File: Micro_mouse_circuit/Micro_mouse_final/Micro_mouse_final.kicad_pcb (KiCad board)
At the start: 2 copper layers, 77.3 x 75 mm, 51 parts, among them J1 Conn_01x02, J2 USB_C_Receptacle_PowerOnly_6P, J3 Conn_02x16_Odd_Even, U1 INA219AxDCN, U10 SN74LVC1G3157DCKR, U11 TPS22917DBVR, U13 TPS22917DBVR, U2 AMS1117-3.3, U3 HUSB237-AA001-DN06R, U4 MT3608, U5 LM2596SX-5_0/NOPB, U6 SK22D15L5, U7 L298N_C19922, U8 L298N_C19922, U9 TP4056_C382139

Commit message: common share
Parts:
- added R9: 0, xxcustom_footprint:C1206, F.Cu at (161.0, 103.5)
- L1: value 10uH -> 10u
- R10: value 0805W8F4702T5E -> 47k
- R12: footprint xxcustom_footprint:C1206 -> xxcustom_footprint:R1206
- R14, R16: footprint xxcustom_footprint:R0402 -> xxcustom_footprint:R1206
- R15: value 6k -> 5.6k
- R3: value 0603WAF7502T5E -> 75k
- R4: value 0805W8F2702T5E -> 27k
- moved C3 28.2 mm to (188.0, 101.0)
- moved REF1 0.50 mm to (150.0, 76.5)
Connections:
- D2 pad 1: Net-(D2-K) -> /SwitchCommon
- L2 pad 1: Net-(D2-K) -> /SwitchCommon
- U5 pad 2: Net-(D2-K) -> /SwitchCommon
- U9 pad 4: Net-(U9-VCC) -> /5V
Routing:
- net GND: track 80.0 -> 0.00 mm
- net /9V: track 46.1 -> 0.00 mm
- net /5V: track 39.8 -> 0.00 mm
- net Net-(D2-K): track 31.5 -> 0.00 mm
- net /BatteryPos: track 26.2 -> 0.00 mm
- net /SwitchOn: track 18.2 -> 0.00 mm
- net Net-(J1-Pin_1): track 14.2 -> 0.00 mm
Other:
- outline, holes or cut-outs redrawn

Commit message: push  - kt
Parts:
- removed REF1: high_frequency_680uF35V, xxcustom_footprint:CAP-TH_BD10.0-P5.00-D1.0-FD
- added C2: 680u, xxcustom_footprint:CAP-TH_BD8.0-P3.50-D0.6-FD, F.Cu at (150.0, 77.0)
- added R11: 1, xxcustom_footprint:R1206, F.Cu at (170.8, 137.6)
- added R13: 1, xxcustom_footprint:R1206, F.Cu at (170.8, 141.0)
- added R9: 1, xxcustom_footprint:R1206, F.Cu at (170.8, 134.3)
- added TP6: TestPoint, TestPoint:TestPoint_Pad_2.5x2.5mm, F.Cu at (163.0, 87.0)
- added TP7: TestPoint, TestPoint:TestPoint_Pad_2.5x2.5mm, F.Cu at (163.0, 91.5)
- added TP8: TestPoint, TestPoint:TestPoint_Pad_2.5x2.5mm, F.Cu at (176.0, 134.9)
- added TP9: TestPoint, TestPoint:TestPoint_Pad_2.5x2.5mm, F.Cu at (176.0, 139.5)
- C1: value CL31B105KBHNNNE -> 1u
- C4: value RVT220UF10V67RV0037 -> 220u
- R17, R6: footprint xxcustom_footprint:C1206 -> xxcustom_footprint:R1206
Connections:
- net /VBoost renamed /5VBoost
- LED1 pad 2: Net-(LED1-A) -> /5V
- LED2 pad 2: Net-(LED1-A) -> /5V

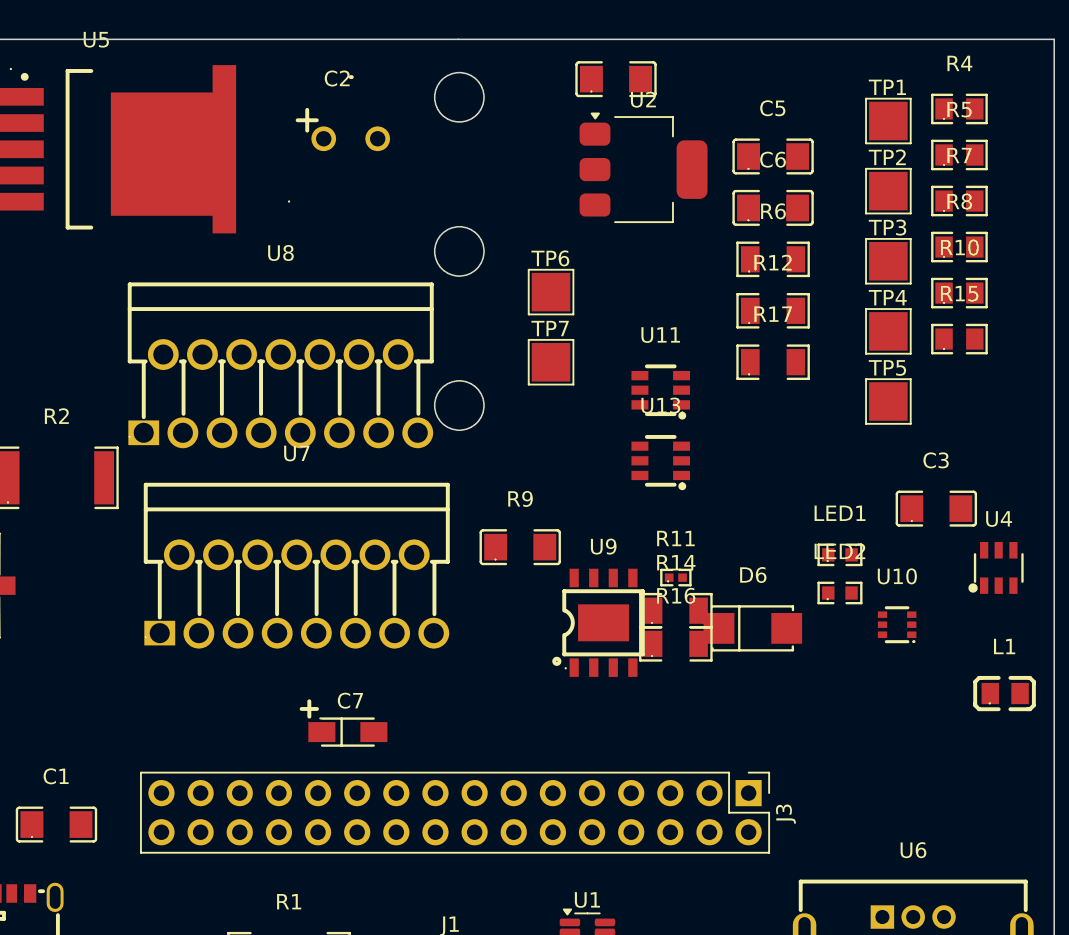
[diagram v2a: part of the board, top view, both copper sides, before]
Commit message: FInal Additions to Schematic
-Added Kill Switch
-Moderated 3.3 Motor Control to 2.4 V
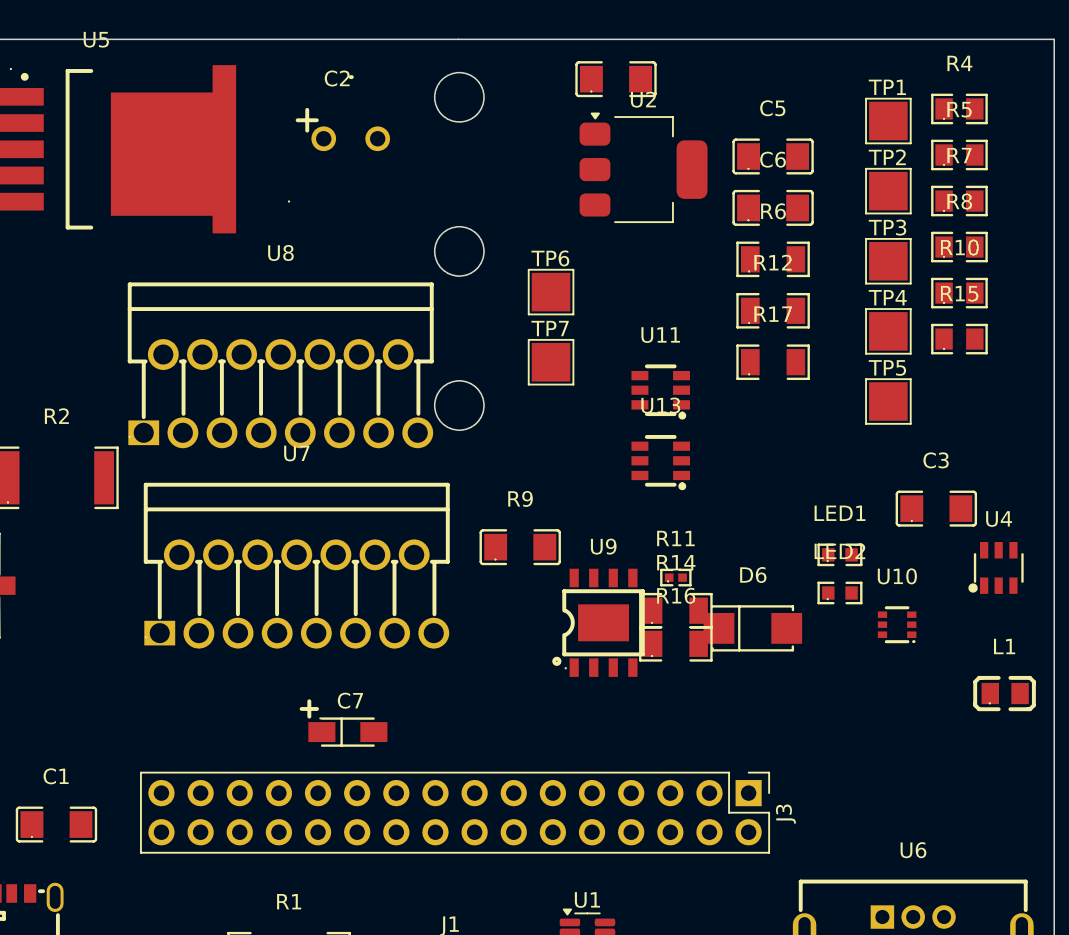
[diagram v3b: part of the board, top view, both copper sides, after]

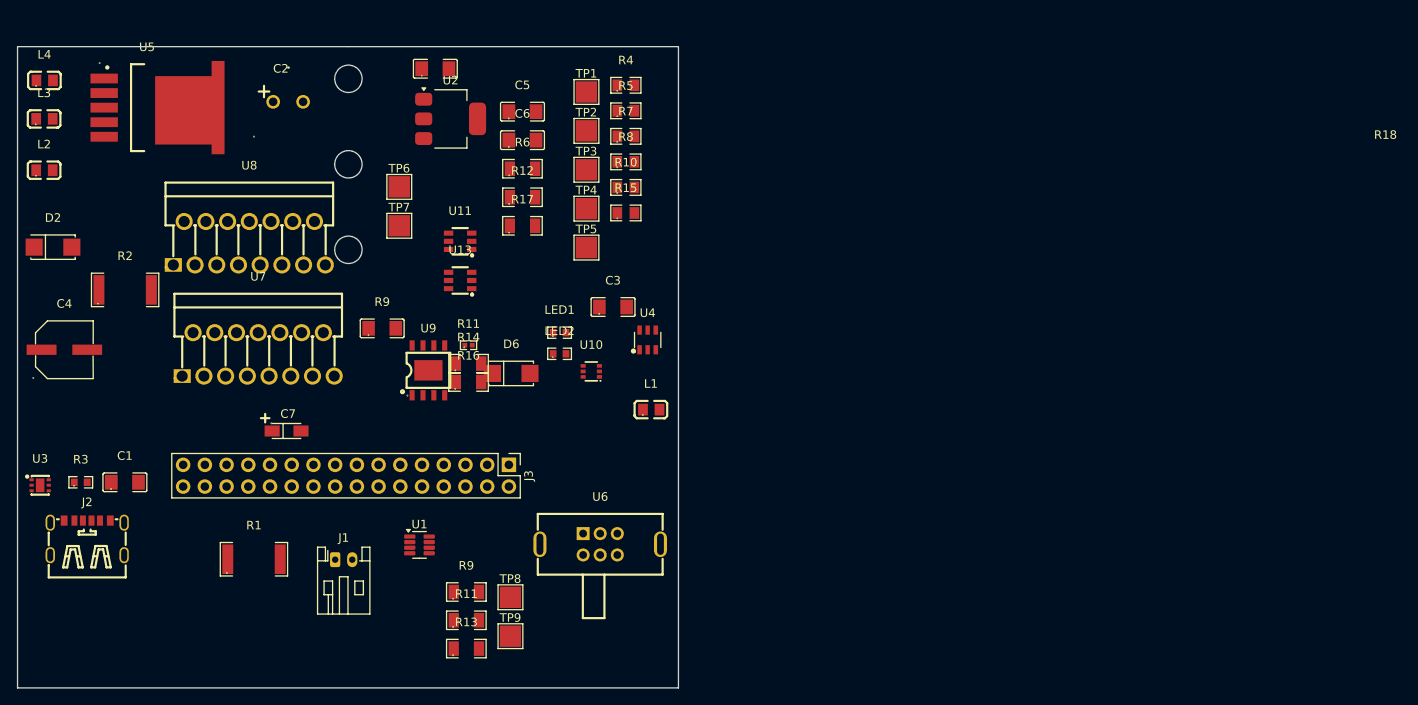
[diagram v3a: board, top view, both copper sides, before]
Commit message: push to Max - switch config finalized
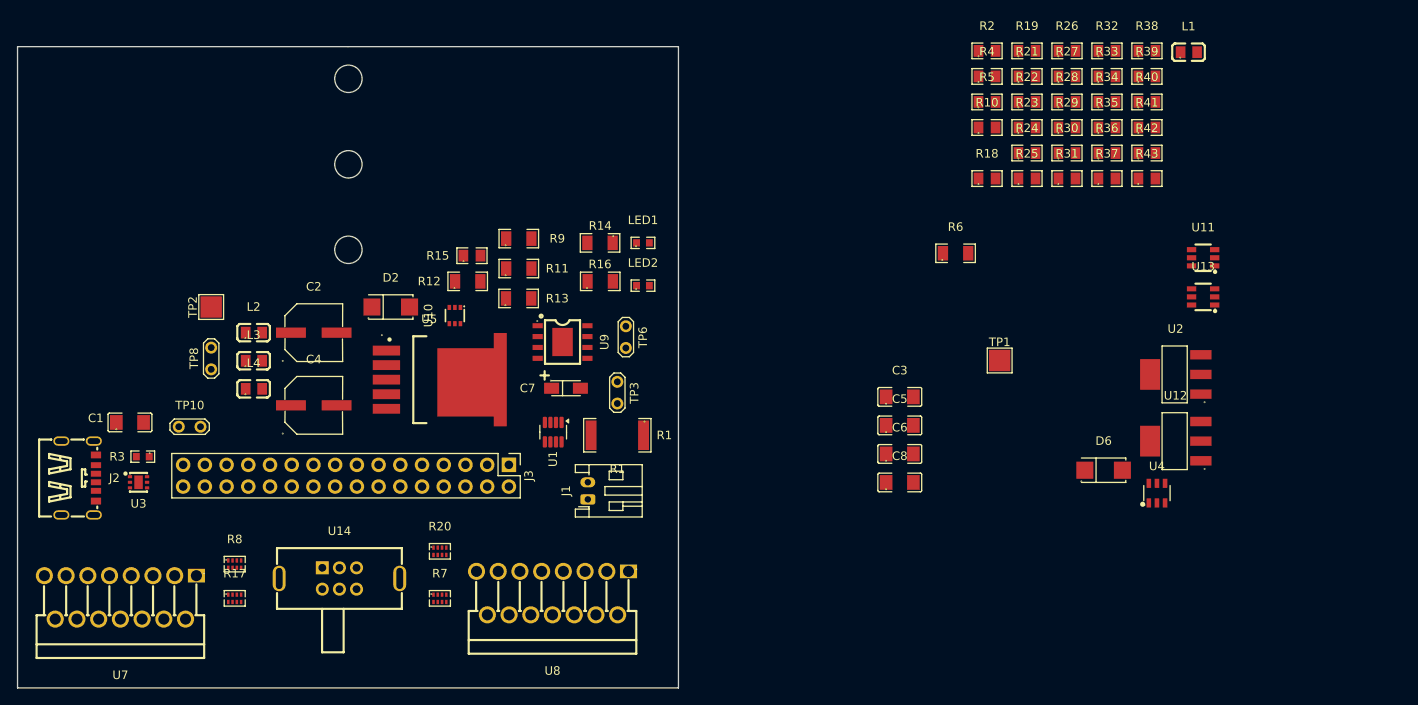
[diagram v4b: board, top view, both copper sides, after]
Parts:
- removed the R11 at (170.8, 137.6)
- removed the R11 at (171.1, 105.5)
- removed the R9 at (170.8, 134.3)
- removed the R9 at (161.0, 103.5)
- removed TP4, TP5, TP7, TP9: TestPoint, TestPoint:TestPoint_Pad_2.5x2.5mm
- removed U6: SK22D15L5, xxcustom_footprint:SW-TH_XKB_SK22D15L7
- added C8: 22u, xxcustom_footprint:C1206, F.Cu at (221.5, 121.5)
- added R11: 1, xxcustom_footprint:R1206, F.Cu at (177.0, 96.5)
- added R19: 47k, xxcustom_footprint:R0805, F.Cu at (236.4, 71.0)
- added R20: RC-MT08W3R0JT, xxcustom_footprint:RES-ARRAY-SMD_0402-8P-L2.0-W1.0-BL, F.Cu at (167.7, 129.6)
- added R21: 47k, xxcustom_footprint:R0805, F.Cu at (236.4, 74.0)
- added R22: 27k, xxcustom_footprint:R0805, F.Cu at (236.4, 77.0)
- added R23: 47k, xxcustom_footprint:R0805, F.Cu at (236.4, 80.0)
- added R24: 27k, xxcustom_footprint:R0805, F.Cu at (236.4, 83.0)
- added R25: 27k, xxcustom_footprint:R0805, F.Cu at (236.4, 86.0)
- added R26: 47k, xxcustom_footprint:R0805, F.Cu at (241.1, 71.0)
- added R27: 27k, xxcustom_footprint:R0805, F.Cu at (241.1, 74.0)
- added R28: 27k, xxcustom_footprint:R0805, F.Cu at (241.1, 77.0)
- added R29: 47k, xxcustom_footprint:R0805, F.Cu at (241.1, 80.0)
- added R30: 27k, xxcustom_footprint:R0805, F.Cu at (241.1, 83.0)
- added R31: 27k, xxcustom_footprint:R0805, F.Cu at (241.1, 86.0)
- added R32: 47k, xxcustom_footprint:R0805, F.Cu at (245.8, 71.0)
- added R33: 27k, xxcustom_footprint:R0805, F.Cu at (245.8, 74.0)
- added R34: 27k, xxcustom_footprint:R0805, F.Cu at (245.8, 77.0)
- added R35: 47k, xxcustom_footprint:R0805, F.Cu at (245.8, 80.0)
- added R36: 27k, xxcustom_footprint:R0805, F.Cu at (245.8, 83.0)
- added R37: 27k, xxcustom_footprint:R0805, F.Cu at (245.8, 86.0)
- added R38: 47k, xxcustom_footprint:R0805, F.Cu at (250.4, 71.0)
- added R39: 27k, xxcustom_footprint:R0805, F.Cu at (250.4, 74.0)
- added R40: 27k, xxcustom_footprint:R0805, F.Cu at (250.4, 77.0)
- added R41: 47k, xxcustom_footprint:R0805, F.Cu at (250.4, 80.0)
- added R42: 27k, xxcustom_footprint:R0805, F.Cu at (250.4, 83.0)
- added R43: 27k, xxcustom_footprint:R0805, F.Cu at (250.4, 86.0)
- added R9: 1, xxcustom_footprint:R1206, F.Cu at (177.0, 93.0)
- added TP10: TestPoint_2Pole, TestPoint:TestPoint_2Pads_Pitch2.54mm_Drill0.8mm, F.Cu at (139.8, 115.0)
- added U12: AMS1117-3.3, xxcustom_footprint:SOT-223-3_L6.5-W3.4-P2.30-LS7.0-BR, F.Cu at (253.8, 116.7)
- added U14: SK22D15L5, xxcustom_footprint:SW-TH_XKB_SK22D15L7, F.Cu at (156.0, 132.7)
- C2: value 680u -> 220u; footprint xxcustom_footprint:CAP-TH_BD8.0-P3.50-D0.6-FD -> xxcustom_footprint:CAP-SMD_BD6.3-L6.6-W6.6-FD
- C3, C5: value 22uF -> 22u
- R17: value 10k -> RC-MT08W3R0JT; footprint xxcustom_footprint:R1206 -> xxcustom_footprint:RES-ARRAY-SMD_0402-8P-L2.0-W1.0-BL
- R18: value 10k -> 27k; footprint xxcustom_footprint:C1206 -> xxcustom_footprint:R0805
- R2: value 0.2 -> 27k; footprint xxcustom_footprint:R2512 -> xxcustom_footprint:R0805
- R5: value 47k -> 8.2k
- R6: value 10k -> 1.2K
- R7, R8: value 47k -> RC-MT08W3R0JT; footprint xxcustom_footprint:R0805 -> xxcustom_footprint:RES-ARRAY-SMD_0402-8P-L2.0-W1.0-BL
- TP3, TP6, TP8: value TestPoint -> TestPoint_2Pole; footprint TestPoint:TestPoint_Pad_2.5x2.5mm -> TestPoint:TestPoint_2Pads_Pitch2.54mm_Drill0.8mm
- U2: footprint Package_TO_SOT_SMD:SOT-223-3_TabPin2 -> xxcustom_footprint:SOT-223-3_L6.5-W3.4-P2.30-LS7.0-BR
- moved R2 104.6 mm to (231.7, 71.0)
- moved U2 89.9 mm to (253.8, 108.9)
- moved U11 86.9 mm to (257.0, 95.2)
- moved U13 86.9 mm to (257.0, 99.8)
- moved L1 75.5 mm to (255.3, 71.2)
- moved D6 70.2 mm to (245.4, 120.1)
- moved R18 65.8 mm to (231.7, 86.0)
- moved R8 65.6 mm to (143.7, 131.1)
- moved U4 62.2 mm to (251.6, 122.8)
- moved R7 58.2 mm to (167.8, 135.1)
- moved TP1 57.6 mm to (233.2, 107.3)
- moved C5 57.4 mm to (221.5, 114.8)
- moved C6 57.4 mm to (221.5, 118.2)
- moved R17 55.1 mm to (143.7, 135.1)
- moved U8 54.1 mm to (180.9, 134.5), turned to 180 degrees
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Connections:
- C2 pad 1: /SwitchCommon -> /5V Regulator Charge
- C3 pad 1: /SwitchOn -> /5VBoostedOn
- C5 pad 1: /5VBoosted -> /5V Out
- C6 pad 1: /5VBoost -> /5V Out
- D2 pad 1: /SwitchCommon -> /5V Regulator Charge
- D6 pad 1: /5VBoosted -> /5V Out
- J3 pad 18: /3V3 oUT -> /3V3 OUT
- L1 pad 1: /SwitchOn -> /5VBoostedOn
- L2 pad 1: /SwitchCommon -> /5V Regulator Charge
- R1 pad 2: Net-(U1-IN+) -> /BatteryPos
- R12 pad 1: GND -> /R_prog
- R15 pad 1: GND -> /R_prog
- R17 pad 1: GND -> unconnected-(R17-Pad1)
- R17 pad 2: Net-(U7-Sense_A) -> unconnected-(R17-Pad2)
- R18 pad 1: GND -> /MOTOR2_CTRL1_2.4
- R18 pad 2: Net-(U8-Sense_A) -> Net-(R18-Pad2)
- R2 pad 1: Net-(LED1-A) -> /3V3 OUT
- R2 pad 2: unconnected-(R2-Pad2) -> Net-(U12-GND)
- R4 pad 1: /V3.3Reg -> /3V3 OUT
- R5 pad 1: /5VBoosted -> /5V Out
- R5 pad 2: GND -> Net-(U4-FB)
- R6 pad 1: GND -> Net-(U4-FB)
- R7 pad 2: Net-(U8-Sense_B) -> Net-(R7-Pad2)
- R8 pad 2: Net-(U7-Sense_B) -> Net-(R8-Pad2)
- TP1 pad 1: /5VBoosted -> /5V Out
- TP2 pad 1: GND -> /5V
- TP3 pad 1: GND -> Net-(J1-Pin_1)
- TP6 pad 1: /SwitchCommon -> /BatteryPos
- TP8 pad 1: Net-(U3-VSET) -> /5V Regulator Charge
- U1 pad 1: Net-(U1-IN+) -> Net-(J1-Pin_1)
- U1 pad 2: Net-(U1-IN-) -> /BatteryPos
- U1 pad 4: /5V -> /5V Out
- U1 pad 8: /5V -> /5V Out
- U10 pad 4: /R_prog -> unconnected-(U10-A-Pad4)
- U2 pad 2: /V3.3Reg -> /3V3 OUT
- U2 pad 3: /5VBoost -> /5V Out
- U4 pad 3: GND -> Net-(U4-FB)
- U4 pad 4: unconnected-(U4-EN-Pad4) -> /5VBoostedOn
- U4 pad 5: /SwitchOn -> /5VBoostedOn
- U5 pad 1: /SwitchCommon -> /5V Regulator Charge
- U5 pad 2: /SwitchCommon -> /5V Regulator Charge
- U5 pad 5: GND -> /BatteryPos
- U7 pad 10: /MOTOR3_CTRL1 -> /MOTOR3_CTRL1_2.4
- U7 pad 11: unconnected-(U7-Enable_B-Pad11) -> /MOTOR3_CTRL1_2.4
- U7 pad 12: /MOTOR3_CTRL2 -> /MOTOR3_CTRL2_2.4
- U7 pad 4: /5VBoosted -> /5V Out
- U7 pad 5: /MOTOR1_CTRL1 -> /MOTOR1_CTRL1_2.4
- U7 pad 6: unconnected-(U7-Enable_A-Pad6) -> /MOTOR1_CTRL1_2.4
- U7 pad 7: /MOTOR1_CTRL2 -> /MOTOR1_CTRL2_2.4
- U7 pad 9: /5VBoosted -> /5V Out
- U8 pad 10: /MOTOR4_CTRL1 -> /MOTOR4_CTRL1_2.4
- U8 pad 11: unconnected-(U8-Enable_B-Pad11) -> /MOTOR4_CTRL1_2.4
- U8 pad 12: /MOTOR4_CTRL2 -> /MOTOR4_CTRL2_2.4
- U8 pad 4: /5VBoosted -> /5V Out
- U8 pad 5: /MOTOR2_CTRL1 -> /MOTOR2_CTRL1_2.4
- U8 pad 6: unconnected-(U8-Enable_A-Pad6) -> /MOTOR2_CTRL1_2.4
- U8 pad 7: /MOTOR2_CTRL2 -> /MOTOR2_CTRL2_2.4
- U8 pad 9: /5VBoosted -> /5V Out

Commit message: common share update
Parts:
- removed C8: 22u, xxcustom_footprint:C1206
- removed TP2: TestPoint, TestPoint:TestPoint_Pad_2.5x2.5mm
- removed U11, U13: TPS22917DBVR, xxcustom_footprint:SOT-23-6_L2.9-W1.6-P0.95-LS2.8-BR
- added R44: 100, xxcustom_footprint:R0805, F.Cu at (162.0, 136.5)
- added R45: 75, xxcustom_footprint:R0603, F.Cu at (168.7, 142.5)
- added TP11: TestPoint, TestPoint:TestPoint_Pad_2.5x2.5mm, F.Cu at (188.0, 81.0)
- added TP12: TestPoint, TestPoint:TestPoint_Pad_2.5x2.5mm, F.Cu at (180.0, 81.5)
- added TP13: TestPoint, TestPoint:TestPoint_Pad_2.5x2.5mm, F.Cu at (172.5, 82.0)
- added TP14: TestPoint, TestPoint:TestPoint_Pad_2.5x2.5mm, F.Cu at (164.5, 86.5)
- added TP15: TestPoint, TestPoint:TestPoint_Pad_2.5x2.5mm, F.Cu at (138.5, 80.0)
- added TP16: TestPoint, TestPoint:TestPoint_Pad_2.5x2.5mm, F.Cu at (140.5, 95.5)
- added TP17: TestPoint, TestPoint:TestPoint_Pad_2.5x2.5mm, F.Cu at (152.0, 77.0)
- added TP18: TestPoint, TestPoint:TestPoint_Pad_2.5x2.5mm, F.Cu at (153.5, 90.0)
- added TP19: TestPoint, TestPoint:TestPoint_Pad_2.5x2.5mm, F.Cu at (150.0, 143.0)
- added TP20: TestPoint, TestPoint:TestPoint_Pad_2.5x2.5mm, F.Cu at (159.0, 143.0)
- added TP4: TestPoint_2Pole, TestPoint:TestPoint_2Pads_Pitch2.54mm_Drill0.8mm, F.Cu at (145.7, 100.2)
- added TP5: TestPoint_2Pole, TestPoint:TestPoint_2Pads_Pitch2.54mm_Drill0.8mm, F.Cu at (150.0, 98.5)
- added U15: S9013_J3, Package_TO_SOT_SMD:SOT-23, F.Cu at (167.9, 136.1)
- added U16: SS8550_C8542, Package_TO_SOT_SMD:SOT-23, F.Cu at (163.9, 140.9)
- added U6: S9013_J3, Package_TO_SOT_SMD:SOT-23, F.Cu at (144.1, 136.5)
- R19: value 47k -> 75; footprint xxcustom_footprint:R0805 -> xxcustom_footprint:R0603
- R2: value 27k -> 100
- U12: value AMS1117-3.3 -> SS8550_C8542; footprint xxcustom_footprint:SOT-223-3_L6.5-W3.4-P2.30-LS7.0-BR -> Package_TO_SOT_SMD:SOT-23
- moved U2 130.7 mm to (125.5, 84.0), turned to 90 degrees
- moved U4 129.0 mm to (125.0, 98.0), turned to -90 degrees
- moved L1 125.0 mm to (132.5, 94.5)
- moved D6 122.9 mm to (125.5, 93.0), turned to 180 degrees
- moved R19 115.0 mm to (145.5, 141.5)
- moved R2 113.7 mm to (142.5, 141.5), turned to -90 degrees
- moved TP1 107.8 mm to (125.5, 110.5)
- moved R33 107.7 mm to (138.5, 83.5)
- moved R34 107.6 mm to (138.5, 86.0)
- moved R32 107.3 mm to (138.5, 75.0)
- moved U12 107.3 mm to (148.6, 137.5)
- moved R36 106.5 mm to (140.5, 99.0)
- moved R37 106.5 mm to (140.5, 102.0)
- moved R35 106.3 mm to (140.0, 91.0)
- moved C6 105.1 mm to (125.0, 76.5)
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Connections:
- C5 pad 1: /5V Out -> /5V
- C6 pad 1: /5V Out -> /5V
- D2 pad 1: /5V Regulator Charge -> Net-(D2-K)
- D6 pad 1: /5V Out -> /5V
- J3 pad 14: /Battery -> /BatteryPos
- J3 pad 20: /5V Out -> /5V
- L2 pad 1: /5V Regulator Charge -> Net-(D2-K)
- LED1 pad 2: /5V -> Net-(LED1-A)
- LED2 pad 2: /5V -> Net-(LED1-A)
- R11 pad 2: /5V -> Net-(LED1-A)
- R13 pad 2: /5V -> Net-(LED1-A)
- R19 pad 1: Net-(U12-GND) -> Net-(U6-E)
- R2 pad 1: /3V3 OUT -> /5V
- R2 pad 2: Net-(U12-GND) -> Net-(U12-B)
- R5 pad 1: /5V Out -> /5V
- R9 pad 2: /5V -> Net-(LED1-A)
- TP1 pad 1: /5V Out -> /5V
- TP8 pad 1: /5V Regulator Charge -> Net-(D2-K)
- U1 pad 4: /5V Out -> /5V
- U1 pad 8: /5V Out -> /5V
- U12 pad 1: Net-(U12-GND) -> Net-(U12-B)
- U12 pad 2: /3V3 OUT -> /5V
- U12 pad 3: /5V -> /EXT_LOAD1_OUT
- U2 pad 3: /5V Out -> /5V
- U5 pad 2: /5V Regulator Charge -> Net-(D2-K)
- U5 pad 5: /BatteryPos -> /5VBoostedOn
- U7 pad 4: /5V Out -> /5V
- U7 pad 9: /5V Out -> /5V
- U8 pad 4: /5V Out -> /5V
- U8 pad 9: /5V Out -> /5V
- U9 pad 4: /5V -> Net-(LED1-A)
- U9 pad 8: /5V -> Net-(LED1-A)
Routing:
- net /5V: track 0.00 -> 307.1 mm, vias 0 -> 12
- net /MOTOR4_CTRL2_2.4: track 0.00 -> 197.8 mm
- net /MOTOR4_CTRL2: track 0.00 -> 144.9 mm, vias 0 -> 2
- net /MOTOR4_CTRL1_2.4: track 0.00 -> 136.1 mm
- net /MOTOR4_CTRL1: track 0.00 -> 131.0 mm, vias 0 -> 2
- net /MOTOR1_CTRL1_2.4: track 0.00 -> 115.2 mm
- net /MOTOR2_CTRL2: track 0.00 -> 114.4 mm, vias 0 -> 2
- net /MOTOR2_CTRL2_2.4: track 0.00 -> 103.0 mm, vias 0 -> 2
- net /Motor4_B_Out: track 0.00 -> 103.0 mm, vias 0 -> 8
- net /5VBoostedOn: track 0.00 -> 101.0 mm, vias 0 -> 4
- net /3V3 OUT: track 0.00 -> 89.2 mm, vias 0 -> 2
- net /MOTOR3_CTRL1_2.4: track 0.00 -> 86.4 mm, vias 0 -> 3
- net /MOTOR2_CTRL1_2.4: track 0.00 -> 85.7 mm, vias 0 -> 2
- net /BatteryPos: track 0.00 -> 84.5 mm, vias 0 -> 2
- net /MOTOR1_CTRL2_2.4: track 0.00 -> 82.2 mm, vias 0 -> 3
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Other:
- board size 77.3 x 75 mm -> 80.3 x 75 mm
